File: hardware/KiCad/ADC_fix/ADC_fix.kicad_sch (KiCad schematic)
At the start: 3 parts, among them U1 MCP3422Axx-xMS, U2 MCP3423x-xUN

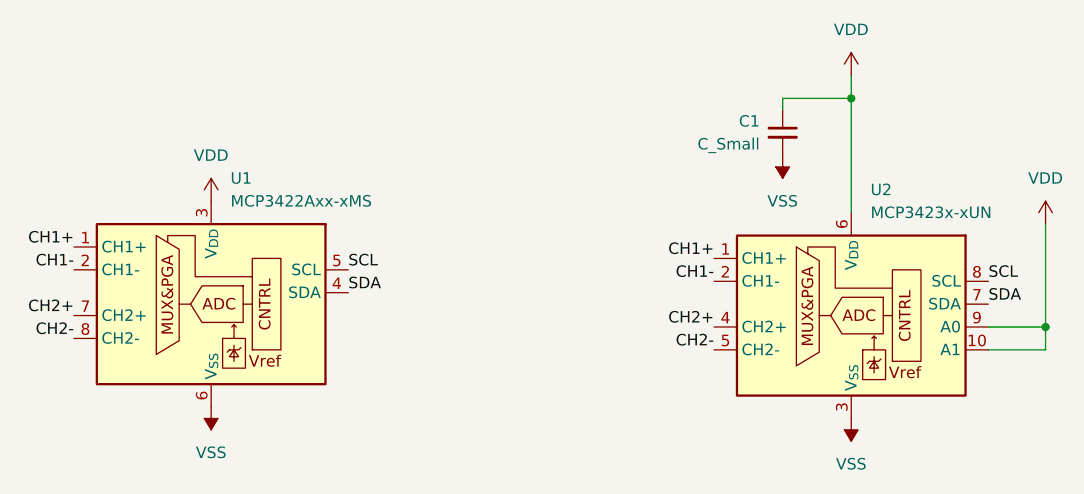
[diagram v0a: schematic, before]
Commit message: Added ADC fix flex PCB design
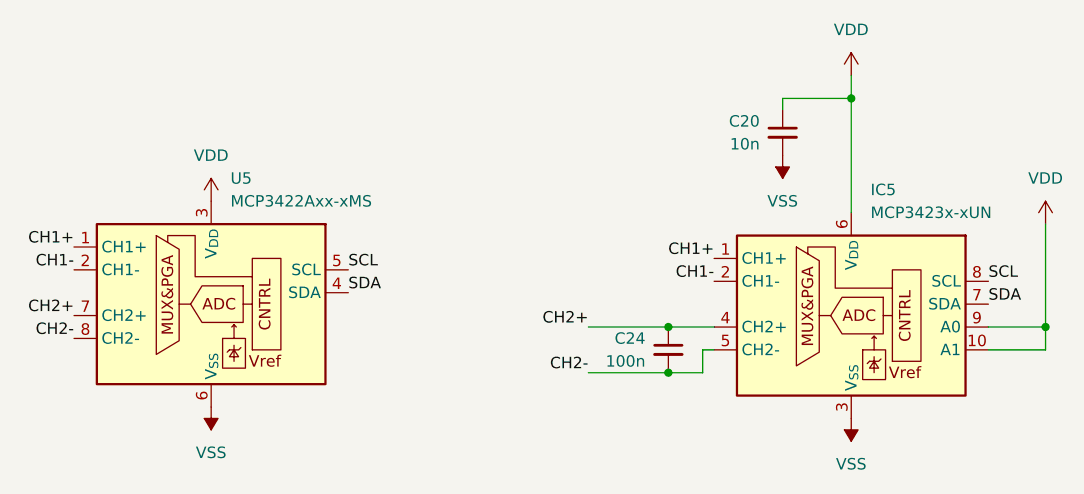
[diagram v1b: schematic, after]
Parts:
- added C24: 100n, Capacitor_SMD:C_0603_1608Metric_Pad1.08x0.95mm_HandSolder, symbol Device:C_Small
- C20: renamed from C1; value C_Small -> 10n
- renumbered U2 to IC5, U1 to U5
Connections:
- net CH2+: now also C24.1
- net CH2-: now also C24.2
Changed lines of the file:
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@@
 		(color 0 0 0 0)
 	)
+	(junction
+		(at 168.91 109.22)
+		(diameter 0)
+		(color 0 0 0 0)
+	)
+	(junction
+		(at 168.91 104.14)
+		(diameter 0)
+		(color 0 0 0 0)
+	)
+	(wire
+		(pts
+			(xy 160.02 104.14) (xy 168.91 104.14)
+		)
+		(stroke
+			(width 0)
+			(type default)
+		)
+	)
+	(wire
+		(pts
+			(xy 172.72 106.68) (xy 173.99 106.68)
+		)
+		(stroke
+			(width 0)
+			(type default)
+		)
+	)
 	(wire
 		(pts
@@
 	(wire
 		(pts
+			(xy 172.72 109.22) (xy 168.91 109.22)
+		)
+		(stroke
+			(width 0)
+			(type default)
+		)
+	)
+	(wire
+		(pts
 			(xy 181.61 80.01) (xy 181.61 78.74)
 		)
@@
 	(wire
 		(pts
+			(xy 160.02 109.22) (xy 168.91 109.22)
+		)
+		(stroke
+			(width 0)
+			(type default)
+		)
+	)
+	(wire
+		(pts
 			(xy 181.61 78.74) (xy 189.23 78.74)
 		)
@@
 			(width 0)
 			(type default)
+		)
+	)
+	(wire
+		(pts
+			(xy 172.72 109.22) (xy 172.72 106.68)
+		)
+		(stroke
+			(width 0)
+			(type default)
+		)
+	)
+	(wire
+		(pts
+			(xy 168.91 104.14) (xy 173.99 104.14)
+		)
+		(stroke
+			(width 0)
+			(type default)
+		)
+	)
+	(label "CH2-"
+		(at 160.02 109.22 180)
+		(effects
+			(font
+				(size 1.27 1.27)
+			)
+			(justify right bottom)
 		)
 	)
@@
 		)
 	)
-	(label "CH2-"
-		(at 173.99 106.68 180)
-		(effects
-			(font
-				(size 1.27 1.27)
-			)
-			(justify right bottom)
-		)
-	)
 	(label "CH1+"
 		(at 102.87 95.25 180)
@@
 	)
 	(label "CH2+"
-		(at 173.99 104.14 180)
+		(at 160.02 104.14 180)
 		(effects
 			(font
@@
 		(dnp no)
 		(fields_autoplaced yes)
-		(property "Reference" "U2"
+		(property "Reference" "IC5"
 			(at 191.3733 88.9 0)
 			(effects
@@
 			(project ""
 				(path "/5f227c3a-1967-496c-a440-4cf1c9ae9084"
-					(reference "U2")
+					(reference "IC5")
 					(unit 1)
 				)
@@
 	)
 	(symbol
+		(lib_id "Device:C_Small")
+		(at 168.91 106.68 0)
+		(unit 1)
+		(exclude_from_sim no)
+		(in_bom yes)
+		(on_board yes)
+		(dnp no)
+		(property "Reference" "C24"
+			(at 166.37 105.4162 0)
+			(effects
+				(font
+					(size 1.27 1.27)
+				)
+				(justify right)
+			)
+		)
+		(property "Value" "100n"
+			(at 166.37 107.9562 0)
+			(effects
+				(font
+					(size 1.27 1.27)
+				)
+				(justify right)
+			)
+		)
+		(property "Footprint" "Capacitor_SMD:C_0603_1608Metric_Pad1.08x0.95mm_HandSolder"
+			(at 168.91 106.68 0)
+			(effects
+				(font
+					(size 1.27 1.27)
+				)
+				(hide yes)
+			)
+		)
+		(property "Datasheet" "~"
+			(at 168.91 106.68 0)
+			(effects
+				(font
+					(size 1.27 1.27)
+				)
+				(hide yes)
+			)
+		)
+		(property "Description" "Unpolarized capacitor, small symbol"
+			(at 168.91 106.68 0)
+			(effects
+				(font
+					(size 1.27 1.27)
+				)
+				(hide yes)
+			)
+		)
+		(pin "2"
+		)
+		(pin "1"
+		)
+		(instances
+			(project "ADC_fix"
+				(path "/5f227c3a-1967-496c-a440-4cf1c9ae9084"
+					(reference "C24")
+					(unit 1)
+				)
+			)
+		)
+	)
+	(symbol
 		(lib_id "power:VDD")
 		(at 189.23 76.2 0)
@@
 		(dnp no)
 		(fields_autoplaced yes)
-		(property "Reference" "U1"
+		(property "Reference" "U5"
 			(at 120.2533 87.63 0)
 			(effects
@@
 			(project ""
 				(path "/5f227c3a-1967-496c-a440-4cf1c9ae9084"
-					(reference "U1")
+					(reference "U5")
 					(unit 1)
 				)
@@
 		(on_board yes)
 		(dnp no)
-		(property "Reference" "C1"
+		(property "Reference" "C20"
 			(at 179.07 81.2862 0)
 			(effects
@@
 			)
 		)
-		(property "Value" "C_Small"
+		(property "Value" "10n"
 			(at 179.07 83.8262 0)
 			(effects
@@
 			(project ""
 				(path "/5f227c3a-1967-496c-a440-4cf1c9ae9084"
-					(reference "C1")
+					(reference "C20")
 					(unit 1)
 				)
